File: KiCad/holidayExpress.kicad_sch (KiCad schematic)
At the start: 23 parts, among them J1 motorPower, J2 motorPower, J3 batteryPower, J4 UARTprogrammer, U1 ESP32-PICO-MINI-02, U2 DRV8833PW, U3 MPM3610GQV-P

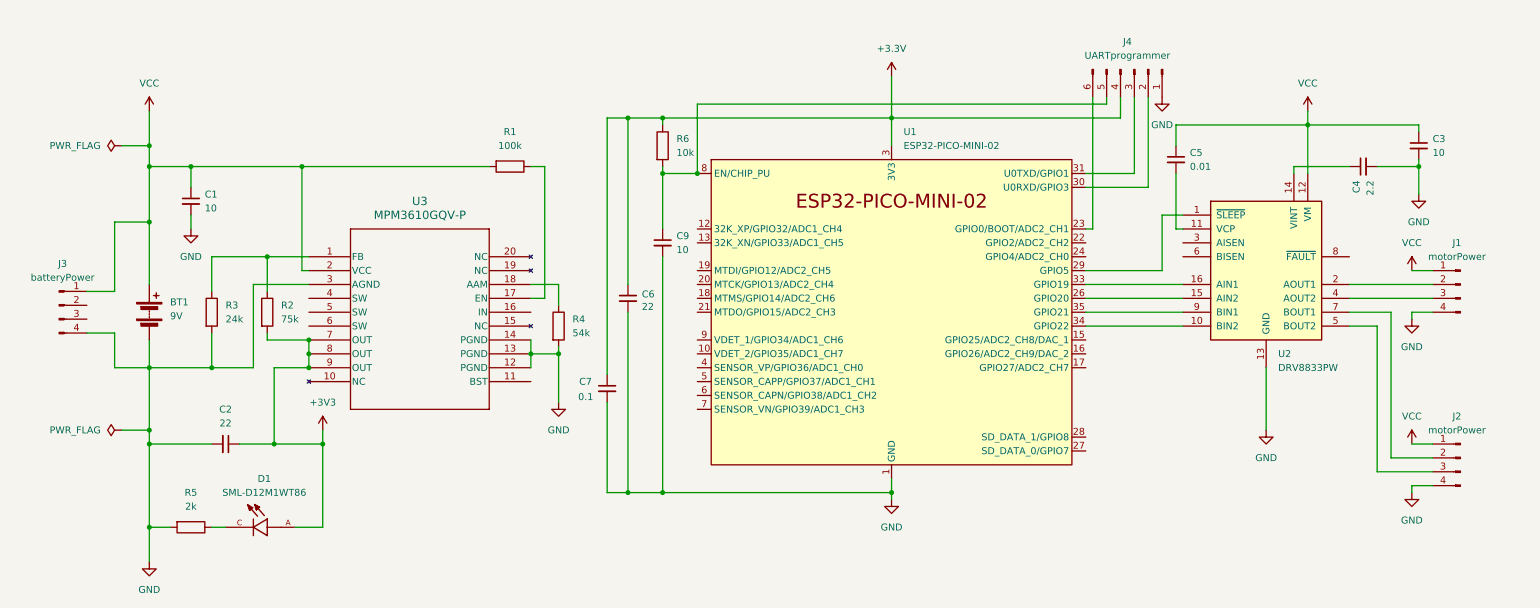
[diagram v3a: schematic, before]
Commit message: complete initial PCB trace routing
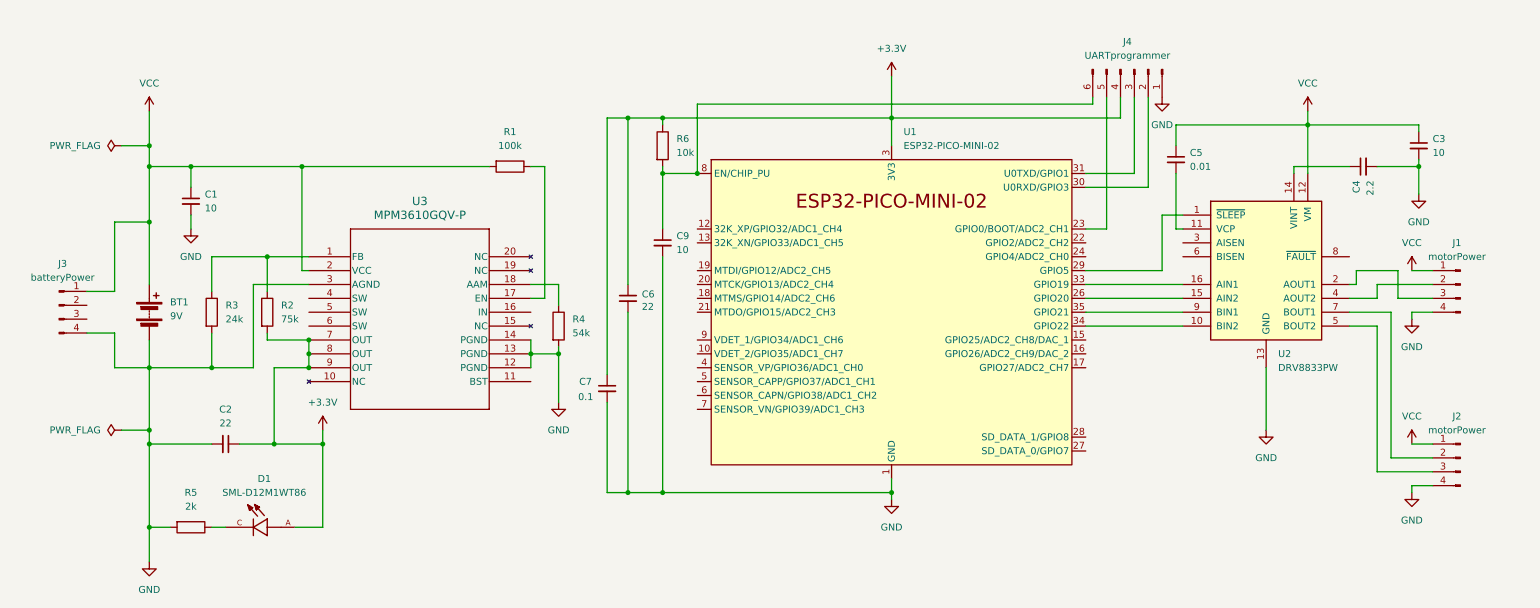
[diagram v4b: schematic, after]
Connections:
- net +3V3 is gone; now on net +3.3V: C2.1, D1.A, R2.2, U3.7 (OUT), U3.8 (OUT), U3.9 (OUT)
- net at C9.1, R6.2, U1.8 (EN/CHIP_PU): now also J4.6 (Pin_6); no longer J4.5 (Pin_5)
- net at J1.2 (Pin_2): now also U2.4 (AOUT2); no longer U2.2 (AOUT1)
- net at J1.3 (Pin_3): now also U2.2 (AOUT1); no longer U2.4 (AOUT2)
- net at U1.23 (GPIO0/BOOT/ADC2_CH1): now also J4.5 (Pin_5); no longer J4.6 (Pin_6)
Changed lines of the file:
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@@
+	(wire
+		(pts
+			(xy 261.62 63.5) (xy 271.78 63.5)
+		)
+		(stroke
+			(width 0)
+			(type default)
+		)
+	)
 	(wire
 		(pts
@@
 	(wire
 		(pts
-			(xy 209.55 29.21) (xy 209.55 53.34)
-		)
-		(stroke
-			(width 0)
-			(type default)
-		)
-	)
-	(wire
-		(pts
 			(xy 68.58 107.95) (xy 63.5 107.95)
 		)
@@
 	(wire
 		(pts
+			(xy 212.09 53.34) (xy 212.09 29.21)
+		)
+		(stroke
+			(width 0)
+			(type default)
+		)
+	)
+	(wire
+		(pts
 			(xy 137.16 30.48) (xy 137.16 43.18)
 		)
@@
 	(wire
 		(pts
-			(xy 212.09 30.48) (xy 212.09 29.21)
-		)
-		(stroke
-			(width 0)
-			(type default)
-		)
-	)
-	(wire
-		(pts
 			(xy 261.62 41.91) (xy 269.24 41.91)
 		)
@@
 	(wire
 		(pts
+			(xy 257.81 63.5) (xy 257.81 60.96)
+		)
+		(stroke
+			(width 0)
+			(type default)
+		)
+	)
+	(wire
+		(pts
 			(xy 106.68 66.04) (xy 109.22 66.04)
 		)
@@
 	(wire
 		(pts
+			(xy 265.43 60.96) (xy 265.43 66.04)
+		)
+		(stroke
+			(width 0)
+			(type default)
+		)
+	)
+	(wire
+		(pts
 			(xy 208.28 43.18) (xy 217.17 43.18)
 		)
@@
 	(wire
 		(pts
+			(xy 209.55 30.48) (xy 209.55 29.21)
+		)
+		(stroke
+			(width 0)
+			(type default)
+		)
+	)
+	(wire
+		(pts
 			(xy 208.28 60.96) (xy 222.25 60.96)
 		)
@@
 	(wire
 		(pts
+			(xy 257.81 60.96) (xy 265.43 60.96)
+		)
+		(stroke
+			(width 0)
+			(type default)
+		)
+	)
+	(wire
+		(pts
 			(xy 48.26 107.95) (xy 50.8 107.95)
 		)
@@
 	(wire
 		(pts
+			(xy 137.16 30.48) (xy 209.55 30.48)
+		)
+		(stroke
+			(width 0)
+			(type default)
+		)
+	)
+	(wire
+		(pts
 			(xy 40.64 107.95) (xy 36.83 107.95)
 		)
@@
 	(wire
 		(pts
-			(xy 256.54 66.04) (xy 271.78 66.04)
-		)
-		(stroke
-			(width 0)
-			(type default)
-		)
-	)
-	(wire
-		(pts
 			(xy 58.42 73.66) (xy 66.04 73.66)
 		)
@@
 	(wire
 		(pts
+			(xy 256.54 63.5) (xy 257.81 63.5)
+		)
+		(stroke
+			(width 0)
+			(type default)
+		)
+	)
+	(wire
+		(pts
 			(xy 246.38 41.91) (xy 256.54 41.91)
 		)
@@
 	(wire
 		(pts
+			(xy 256.54 66.04) (xy 261.62 66.04)
+		)
+		(stroke
+			(width 0)
+			(type default)
+		)
+	)
+	(wire
+		(pts
 			(xy 36.83 41.91) (xy 44.45 41.91)
 		)
@@
 	(wire
 		(pts
-			(xy 256.54 63.5) (xy 271.78 63.5)
-		)
-		(stroke
-			(width 0)
-			(type default)
-		)
-	)
-	(wire
-		(pts
 			(xy 64.77 41.91) (xy 64.77 60.96)
 		)
@@
 	(wire
 		(pts
-			(xy 209.55 53.34) (xy 208.28 53.34)
+			(xy 208.28 53.34) (xy 212.09 53.34)
 		)
 		(stroke
@@
 	(wire
 		(pts
-			(xy 137.16 30.48) (xy 212.09 30.48)
-		)
-		(stroke
-			(width 0)
-			(type default)
-		)
-	)
-	(wire
-		(pts
 			(xy 130.81 43.18) (xy 137.16 43.18)
 		)
@@
 	(wire
 		(pts
+			(xy 265.43 66.04) (xy 271.78 66.04)
+		)
+		(stroke
+			(width 0)
+			(type default)
+		)
+	)
+	(wire
+		(pts
 			(xy 106.68 63.5) (xy 111.76 63.5)
 		)
@@
 		(pts
 			(xy 111.76 85.09) (xy 111.76 76.2)
+		)
+		(stroke
+			(width 0)
+			(type default)
+		)
+	)
+	(wire
+		(pts
+			(xy 261.62 66.04) (xy 261.62 63.5)
 		)
 		(stroke
@@
 	)
 	(symbol
-		(lib_id "power:+3V3")
-		(at 68.58 90.17 0)
-		(unit 1)
-		(exclude_from_sim no)
-		(in_bom yes)
-		(on_board yes)
-		(dnp no)
-		(fields_autoplaced yes)
-		(property "Reference" "#PWR06"
-			(at 68.58 93.98 0)
-			(effects
-				(font
-					(size 1.27 1.27)
-				)
-				(hide yes)
-			)
-		)
-		(property "Value" "+3V3"
-			(at 68.58 85.09 0)
-			(effects
-				(font
-					(size 1.27 1.27)
-				)
-			)
-		)
-		(property "Footprint" ""
-			(at 68.58 90.17 0)
-			(effects
-				(font
-					(size 1.27 1.27)
-				)
-				(hide yes)
-			)
-		)
-		(property "Datasheet" ""
-			(at 68.58 90.17 0)
-			(effects
-				(font
-					(size 1.27 1.27)
-				)
-				(hide yes)
-			)
-		)
-		(property "Description" "Power symbol creates a global label with name \"+3V3\""
-			(at 68.58 90.17 0)
-			(effects
-				(font
-					(size 1.27 1.27)
-				)
-				(hide yes)
-			)
-		)
-		(pin "1"
-		)
-		(instances
-			(project ""
-				(path "/c3dabb1a-9ea8-4f8f-9e0b-7c4553d29435"
-					(reference "#PWR06")
-					(unit 1)
-				)
-			)
-		)
-	)
-	(symbol
 		(lib_id "Device:C_Small")
 		(at 269.24 38.1 0)
@@
 					(unit 1)
 				)
+			)
+		)
+	)
+	(symbol
+		(lib_id "power:+3.3V")
+		(at 68.58 90.17 0)
+		(unit 1)
+		(exclude_from_sim no)
+		(in_bom yes)
+		(on_board yes)
+		(dnp no)
+		(fields_autoplaced yes)
+		(property "Reference" "#PWR016"
+			(at 68.58 93.98 0)
+			(effects
+				(font
+					(size 1.27 1.27)
+				)
+				(hide yes)
+			)
+		)
+		(property "Value" "+3.3V"
+			(at 68.58 85.09 0)
+			(effects
+				(font
+					(size 1.27 1.27)
+				)
+			)
+		)
+		(property "Footprint" ""
+			(at 68.58 90.17 0)
+			(effects
+				(font
+					(size 1.27 1.27)
+				)
+				(hide yes)
+			)
+		)
+		(property "Datasheet" ""
+			(at 68.58 90.17 0)
+			(effects
+				(font
+					(size 1.27 1.27)
+				)
+				(hide yes)
+			)
+		)
+		(property "Description" "Power symbol creates a global label with name \"+3.3V\""
+			(at 68.58 90.17 0)
+			(effects
+				(font
+					(size 1.27 1.27)
+				)
+				(hide yes)
+			)
+		)
+		(pin "1"
+		)
+		(instances
+			(project ""
+				(path "/c3dabb1a-9ea8-4f8f-9e0b-7c4553d29435"
+					(reference "#PWR016")
+					(unit 1)
+				)

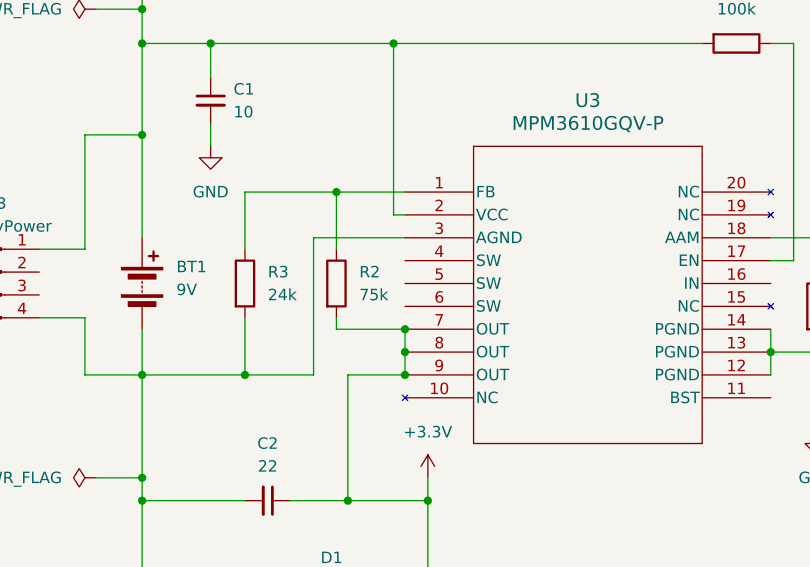
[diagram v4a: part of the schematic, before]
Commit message: adjust clearances and start DRC fixes
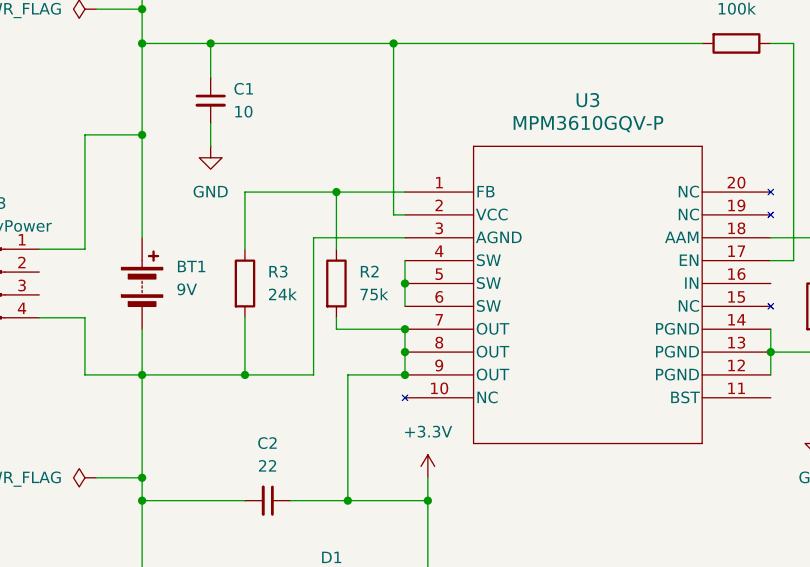
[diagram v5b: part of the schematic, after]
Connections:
- net at U3.4 (SW): now also U3.5 (SW), U3.6 (SW)
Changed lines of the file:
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@@
 		(color 0 0 0 0)
 	)
+	(junction
+		(at 66.04 68.58)
+		(diameter 0)
+		(color 0 0 0 0)
+	)
 	(wire
 		(pts
@@
 	(wire
 		(pts
+			(xy 66.04 68.58) (xy 66.04 71.12)
+		)
+		(stroke
+			(width 0)
+			(type default)
+		)
+	)
+	(wire
+		(pts
 			(xy 68.58 107.95) (xy 63.5 107.95)
 		)
@@
 		)
 		(stroke
+			(width 0)
+			(type default)
+		)
+	)
+	(wire
+		(pts
+			(xy 66.04 66.04) (xy 66.04 68.58)
+		)
+		(stroke

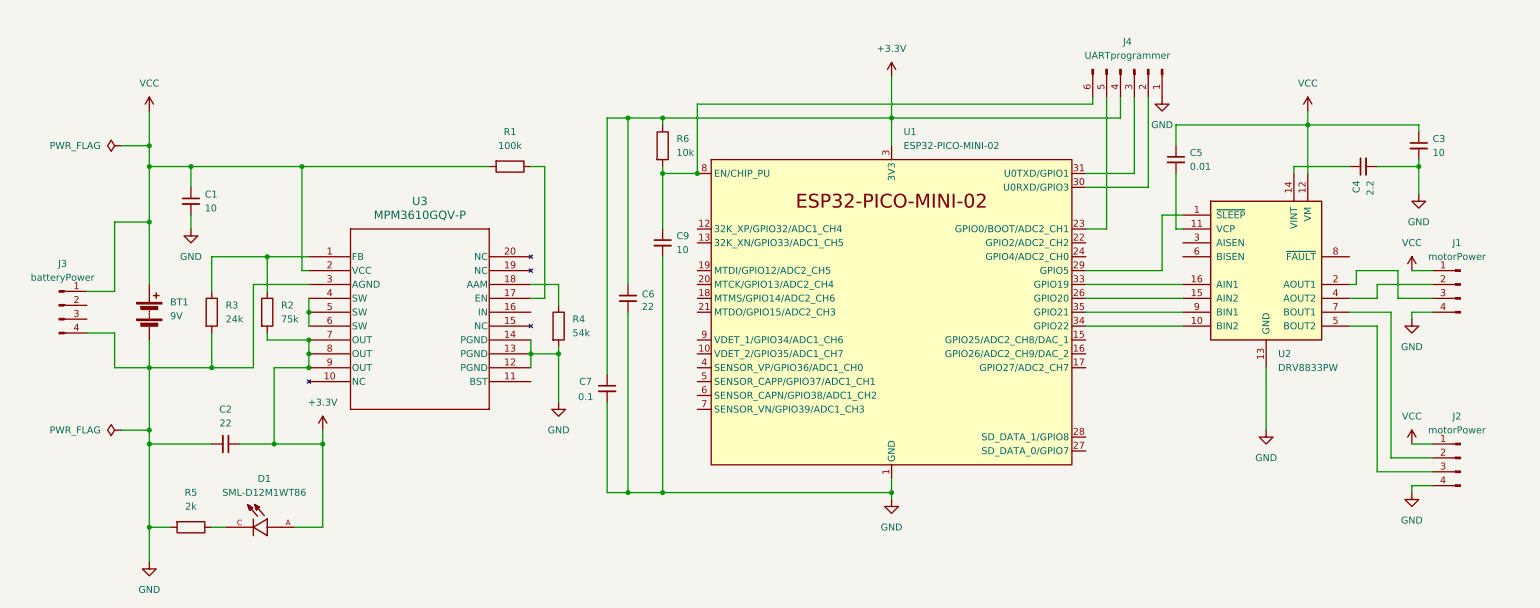
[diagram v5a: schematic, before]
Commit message: add LCSC part numbers to symbols
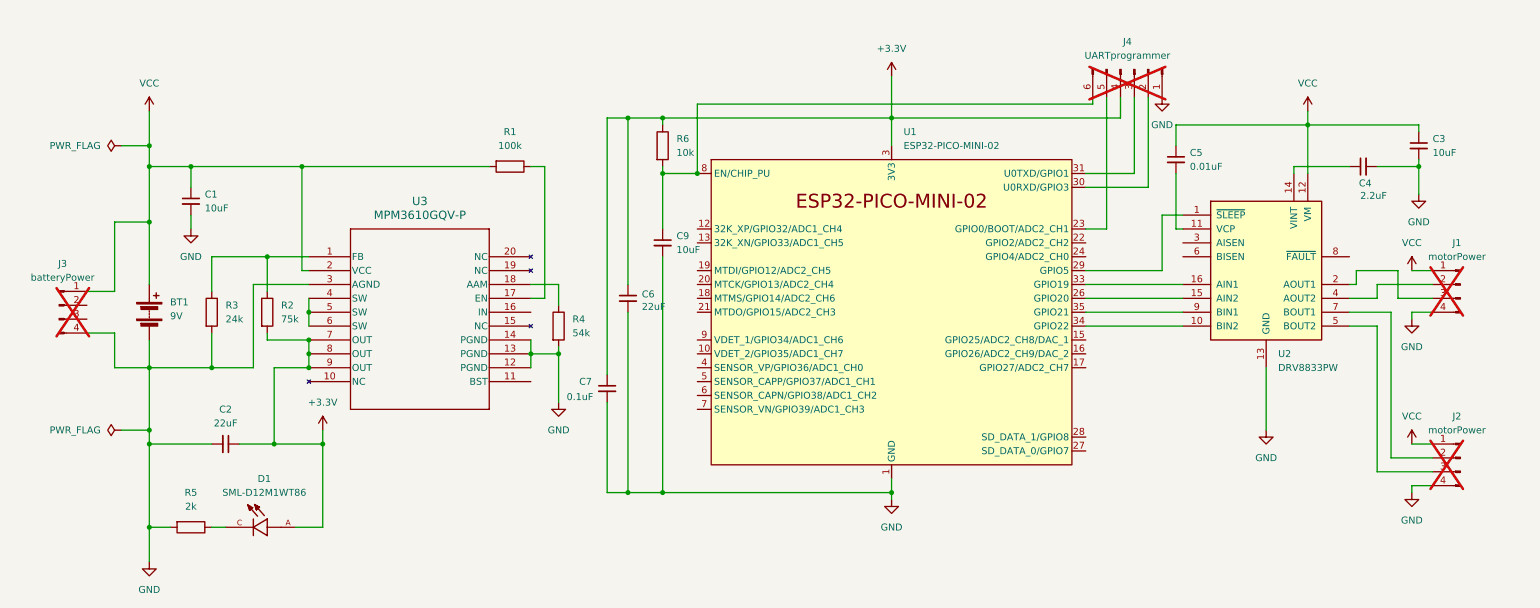
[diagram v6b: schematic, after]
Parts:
- BT1: now left out of the parts list
- C1, C3, C9: value 10 -> 10uF; LCSC Part # (none) -> C7472949
- C2, C6: value 22 -> 22uF; LCSC Part # (none) -> C3845593
- C4: value 2.2 -> 2.2uF; LCSC Part # (none) -> C107369
- C5: value 0.01 -> 0.01uF; LCSC Part # (none) -> C541371
- C7: value 0.1 -> 0.1uF; LCSC Part # (none) -> C6955083
- D1: LCSC Part # (none) -> C2922668
- J1, J2, J3, J4: now not fitted; now left out of the parts list
- R1: LCSC Part # (none) -> C60491
- R2: LCSC Part # (none) -> C137935
- R3: LCSC Part # (none) -> C2933082
- R4: LCSC Part # (none) -> C852840
- R5: LCSC Part # (none) -> C60488
- R6: LCSC Part # (none) -> C60490
- U1: LCSC Part # (none) -> C2980306
- U2: LCSC Part # (none) -> C50506
- U3: LCSC Part # (none) -> C5183856
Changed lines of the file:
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@@
 			)
 		)
-		(property "Value" "10"
+		(property "Value" "10uF"
 			(at 46.99 49.5362 0)
 			(effects
@@
 		)
 		(property "Description" "Unpolarized capacitor, small symbol"
+			(at 44.45 48.26 0)
+			(effects
+				(font
+					(size 1.27 1.27)
+				)
+				(hide yes)
+			)
+		)
+		(property "LCSC Part #" "C7472949"
 			(at 44.45 48.26 0)
 			(effects
@@
 		(dnp no)
 		(property "Reference" "C4"
-			(at 257.8162 44.45 0)
+			(at 260.604 44.958 90)
 			(effects
 				(font
@@
 			)
 		)
-		(property "Value" "2.2"
-			(at 260.3562 44.45 0)
+		(property "Value" "2.2uF"
+			(at 263.398 47.244 90)
 			(effects
 				(font
@@
 			)
 		)
+		(property "LCSC Part #" "C107369"
+			(at 259.08 41.91 90)
+			(effects
+				(font
+					(size 1.27 1.27)
+				)
+				(hide yes)
+			)
+		)
 		(pin "1"
 		)
@@
 			)
 		)
-		(property "Value" "0.1"
+		(property "Value" "0.1uF"
 			(at 118.11 84.074 0)
 			(effects
@@
 		)
 		(property "Description" "Unpolarized capacitor, small symbol"
+			(at 120.65 82.55 0)
+			(effects
+				(font
+					(size 1.27 1.27)
+				)
+				(hide yes)
+			)
+		)
+		(property "LCSC Part #" "C6955083"
 			(at 120.65 82.55 0)
 			(effects
@@
 			)
 		)
-		(property "Value" "10"
+		(property "Value" "10uF"
 			(at 271.78 39.3762 0)
 			(effects
@@
 		)
 		(property "Description" "Unpolarized capacitor, small symbol"
+			(at 269.24 38.1 0)
+			(effects
+				(font
+					(size 1.27 1.27)
+				)
+				(hide yes)
+			)
+		)
+		(property "LCSC Part #" "C7472949"
 			(at 269.24 38.1 0)
 			(effects
@@
 			)
 		)
+		(property "LCSC Part #" " C852840"
+			(at 111.76 71.12 0)
+			(effects
+				(font
+					(size 1.27 1.27)
+				)
+				(hide yes)
+			)
+		)
 		(pin "1"
 		)
@@
 			)
 		)
+		(property "LCSC Part #" "C2922668"
+			(at 55.88 107.95 0)
+			(effects
+				(font
+					(size 1.27 1.27)
+				)
+				(hide yes)
+			)
+		)
 		(pin "A"
 		)
@@
 			)
 		)
-		(property "Value" "10"
+		(property "Value" "10uF"
 			(at 133.35 57.1562 0)
 			(effects
@@
 		)
 		(property "Description" "Unpolarized capacitor, small symbol"
+			(at 130.81 55.88 0)
+			(effects
+				(font
+					(size 1.27 1.27)
+				)
+				(hide yes)
+			)
+		)
+		(property "LCSC Part #" "C7472949"
 			(at 130.81 55.88 0)
 			(effects
@@
 			)
 		)
+		(property "LCSC Part #" "C60491"
+			(at 102.87 41.91 90)
+			(effects
+				(font
+					(size 1.27 1.27)
+				)
+				(hide yes)
+			)
+		)
 		(pin "2"
 		)
@@
 			)
 		)
-		(property "Value" "22"
+		(property "Value" "22uF"
 			(at 127 67.564 0)
 			(effects
@@
 		)
 		(property "Description" "Unpolarized capacitor, small symbol"
+			(at 124.46 66.04 0)
+			(effects
+				(font
+					(size 1.27 1.27)
+				)
+				(hide yes)
+			)
+		)
+		(property "LCSC Part #" "C3845593"
 			(at 124.46 66.04 0)
 			(effects
@@
 			)
 		)
-		(property "Value" "22"
+		(property "Value" "22uF"
 			(at 50.7936 88.9 90)
 			(effects
@@
 		(property "Description" "Unpolarized capacitor, small symbol"
 			(at 50.8 92.71 0)
+			(effects
+				(font
+					(size 1.27 1.27)
+				)
+				(hide yes)
+			)
+		)
+		(property "LCSC Part #" "C3845593"
+			(at 50.8 92.71 90)
 			(effects
 				(font
@@
 		(unit 1)
 		(exclude_from_sim no)
-		(in_bom yes)
-		(on_board yes)
-		(dnp no)
+		(in_bom no)
+		(on_board yes)
+		(dnp yes)
 		(property "Reference" "J1"
 			(at 276.225 55.88 0)
@@
 			)
 		)
+		(property "LCSC Part #" " C60490"
+			(at 130.81 38.1 0)
+			(effects
+				(font
+					(size 1.27 1.27)
+				)
+				(hide yes)
+			)
+		)
 		(pin "1"
 		)
@@
 			)
 		)
+		(property "LCSC Part #" "C2980306"
+			(at 172.72 68.58 0)
+			(effects
+				(font
+					(size 1.27 1.27)
+				)
+				(hide yes)
+			)
+		)
 		(pin "14"
 		)
@@
 			)
 		)
-		(property "Value" "0.01"
+		(property "Value" "0.01uF"
 			(at 227.33 41.9162 0)
 			(effects
@@
 			)
 		)
+		(property "LCSC Part #" "C541371"
+			(at 224.79 40.64 0)
+			(effects
+				(font
+					(size 1.27 1.27)
+				)
+				(hide yes)
+			)
+		)
 		(pin "1"
 		)
@@
 		(unit 1)
 		(exclude_from_sim no)
-		(in_bom yes)
-		(on_board yes)
-		(dnp no)
+		(in_bom no)
+		(on_board yes)
+		(dnp yes)
 		(fields_autoplaced yes)
 		(property "Reference" "J4"
@@
 		(unit 1)
 		(exclude_from_sim no)
-		(in_bom yes)
+		(in_bom no)
 		(on_board no)
 		(dnp no)
@@
 		(unit 1)
 		(exclude_from_sim no)
-		(in_bom yes)
-		(on_board yes)
-		(dnp no)
+		(in_bom no)
+		(on_board yes)
+		(dnp yes)
 		(property "Reference" "J3"
 			(at 20.955 59.69 0)
@@
 			)
 		)
+		(property "LCSC Part #" "C2933082"
+			(at 48.26 68.58 0)
+			(effects
+				(font
+					(size 1.27 1.27)
+				)
+				(hide yes)
+			)
+		)
 		(pin "2"
 		)
@@
 		(unit 1)
 		(exclude_from_sim no)
-		(in_bom yes)
-		(on_board yes)
-		(dnp no)
+		(in_bom no)
+		(on_board yes)
+		(dnp yes)
 		(property "Reference" "J2"
 			(at 276.225 87.63 0)
@@
 			)
 		)
+		(property "LCSC Part #" "C50506"
+			(at 241.3 60.96 0)
+			(effects
+				(font
+					(size 1.27 1.27)
+				)
+				(hide yes)
+			)
+		)
 		(pin "10"
 		)
@@
 			)
 		)
+		(property "LCSC Part #" "C5183856"
+			(at 66.04 58.42 0)
+			(effects
+				(font
+					(size 1.27 1.27)
+				)
+				(hide yes)
+			)
+		)
 		(pin "13"
 		)
@@
 			)
 		)
+		(property "LCSC Part #" " C137935"
+			(at 58.42 68.58 0)
+			(effects
+				(font
+					(size 1.27 1.27)
+				)
+				(hide yes)
+			)
+		)
 		(pin "1"
 		)
@@
 			(effects
 				(font
+					(size 1.27 1.27)
+				)
+				(hide yes)
+			)
+		)
+		(property "LCSC Part #" "C60488"
+			(at 44.45 107.95 90)
+			(effects
+				(font
